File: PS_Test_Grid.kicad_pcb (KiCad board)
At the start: 2 copper layers, 51 parts, among them J1 CONN_01X03, J10 CONN_01X01, J2 CONN_01X01, J3 CONN_01X01, J4 CONN_01X01, J5 CONN_01X01, J6 CONN_01X03, J7 CONN_01X01, J8 CONN_01X01, J9 CONN_01X01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

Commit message: moved test points and cleaned schematic
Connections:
- C11 pad 2: Net-(C11-Pad2) -> /OUT_2-3
- C4 pad 2: Net-(C4-Pad2) -> /OUT_1-3
- J4 pad 1: /OUT_1-2 -> /OUT_1-3
- J9 pad 1: /OUT_2-2 -> /OUT_2-3
- R11 pad 1: Net-(C4-Pad2) -> /OUT_1-3
- R19 pad 1: Net-(C11-Pad2) -> /OUT_2-3
- U2 pad 1: Net-(C4-Pad2) -> /OUT_1-3
- U3 pad 1: Net-(C11-Pad2) -> /OUT_2-3

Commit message: upgraded to KiCad 5
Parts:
- R1, R2, R6, R7: footprint Capacitors_SMD:C_0603 -> Capacitors_SMD:C_0402
- R11: value R -> 330K
- R13, R14, R17: value R -> 100K
- R3, R4, R9: value R -> 220K
- moved U1 4.07 mm to (133.8, 88.5)

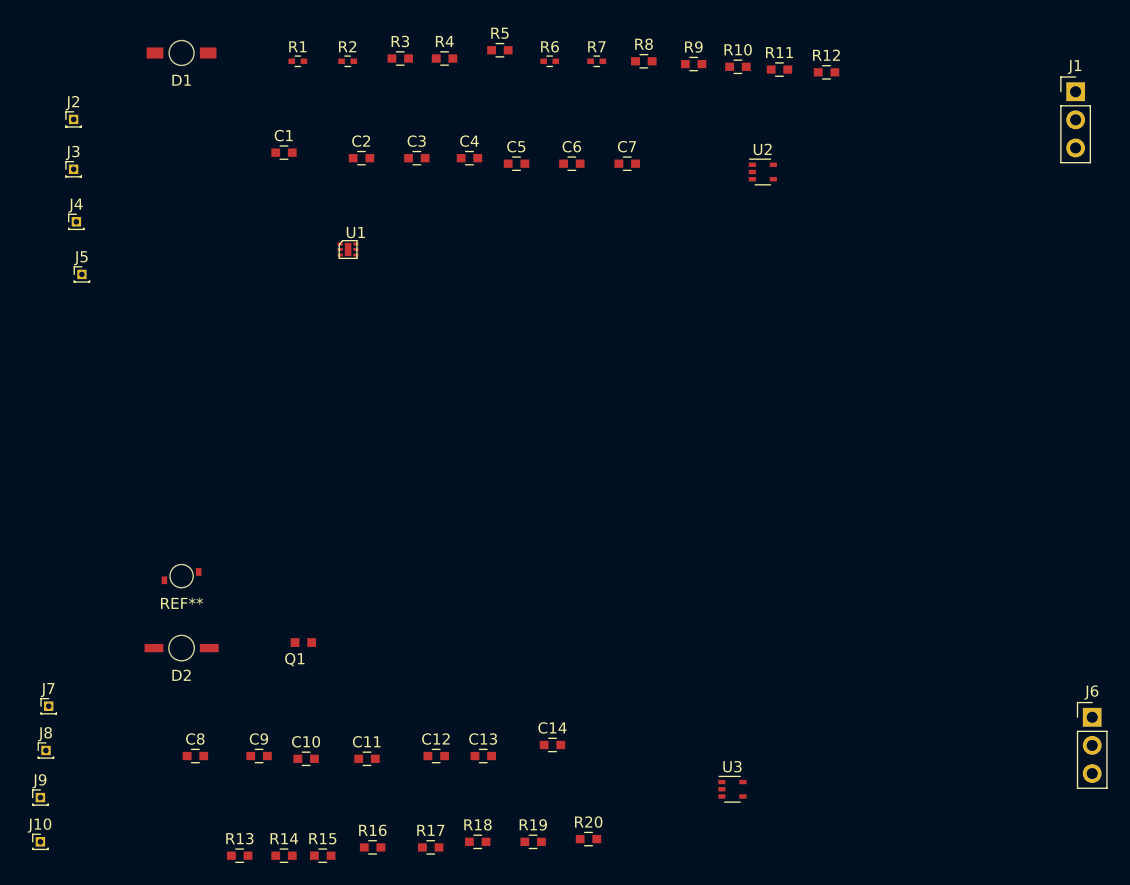
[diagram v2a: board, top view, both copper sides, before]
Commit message: Layout Circuit Add Protection Diode to Schem
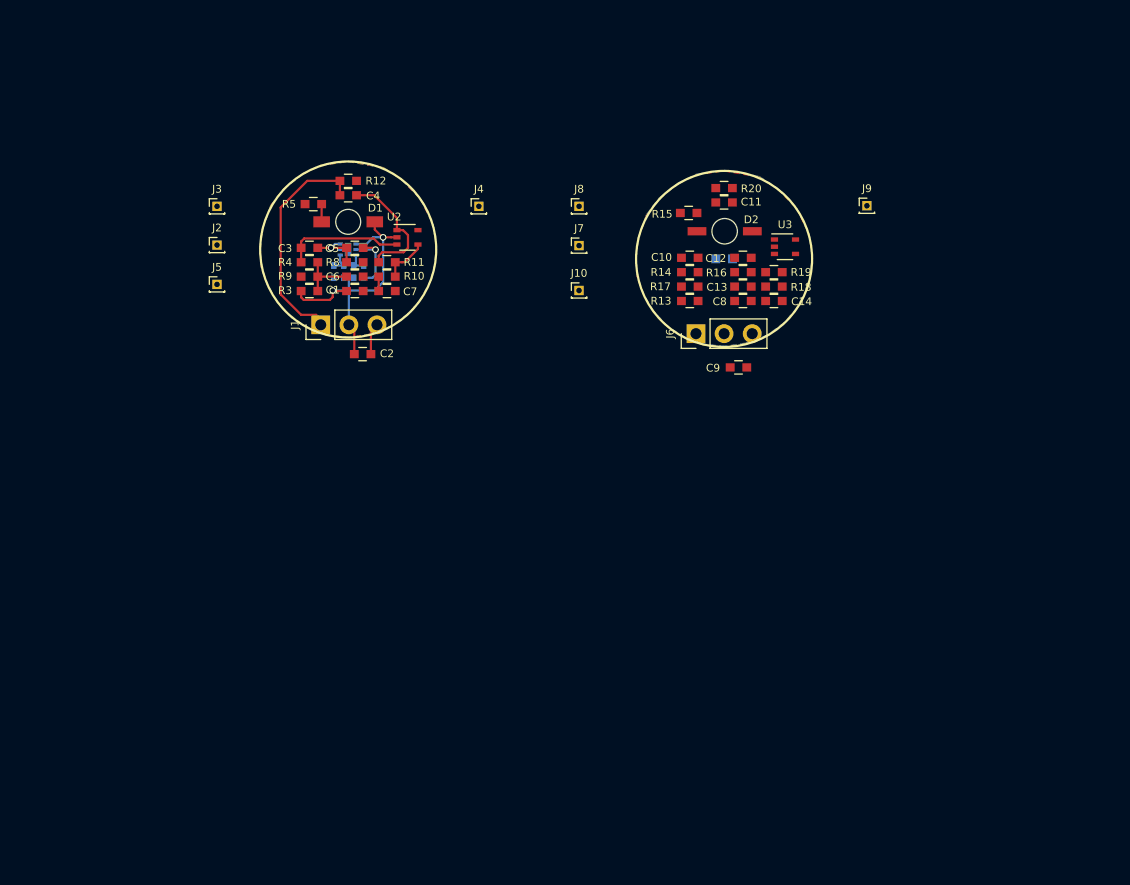
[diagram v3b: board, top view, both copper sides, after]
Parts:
- removed REF**: LSP47F LED, Solutions:LSP47F_LED
- Q1, R1, R2, R6, R7, U1: moved to B.Cu
- moved J9 91.8 mm to (180.7, 84.5)
- moved J1 71.4 mm to (131.3, 95.3), turned to 90 degrees
- moved J10 69.6 mm to (154.7, 92.2)
- moved J8 68.8 mm to (154.7, 84.6)
- moved R15 66.8 mm to (164.6, 85.2), turned to 180 degrees
- moved R13 64.5 mm to (164.7, 93.2)
- moved C8 64.3 mm to (169.4, 93.2)
- moved R14 64.2 mm to (164.7, 90.5)
- moved J7 63.4 mm to (154.7, 88.2)
- moved D2 61.8 mm to (167.8, 86.8)
- moved R16 61.8 mm to (169.4, 90.5)
- moved R20 60.1 mm to (167.8, 83.0)
- moved C11 59.7 mm to (167.8, 84.2)
- moved C10 57.0 mm to (164.7, 89.2)
- moved R18 56.8 mm to (172.2, 91.8), turned to 180 degrees
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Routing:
- net VDD: track 0.00 -> 28.5 mm, vias 0 -> 2
- net /S_1: track 0.00 -> 20.5 mm
- net /OUT_1-3: track 0.00 -> 11.5 mm
- net /OUT_1-2: track 0.00 -> 10.9 mm
- net GND: track 0.00 -> 9.28 mm, vias 0 -> 1
- net Net-(C6-Pad1): track 0.00 -> 5.20 mm
- net /OUT_1-1: track 0.00 -> 4.87 mm, vias 0 -> 1
- net Net-(R10-Pad1): track 0.00 -> 4.25 mm
- net Net-(R2-Pad2): track 0.00 -> 1.98 mm
- net Net-(R1-Pad2): track 0.00 -> 1.93 mm
- net Net-(D1-Pad1): track 0.00 -> 1.60 mm
- net Net-(C7-Pad1): track 0.00 -> 1.30 mm
- added copper zone on B.Cu, net GND
- added copper zone on F.Cu, net GND

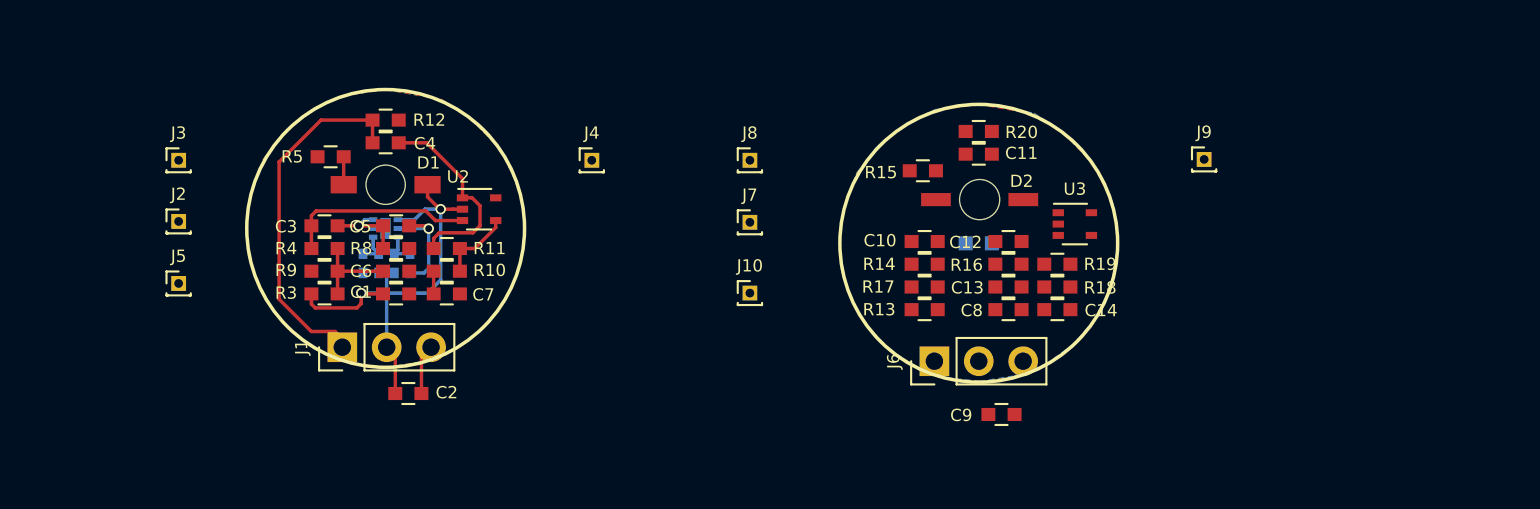
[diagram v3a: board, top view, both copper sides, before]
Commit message: laid out all drc pass
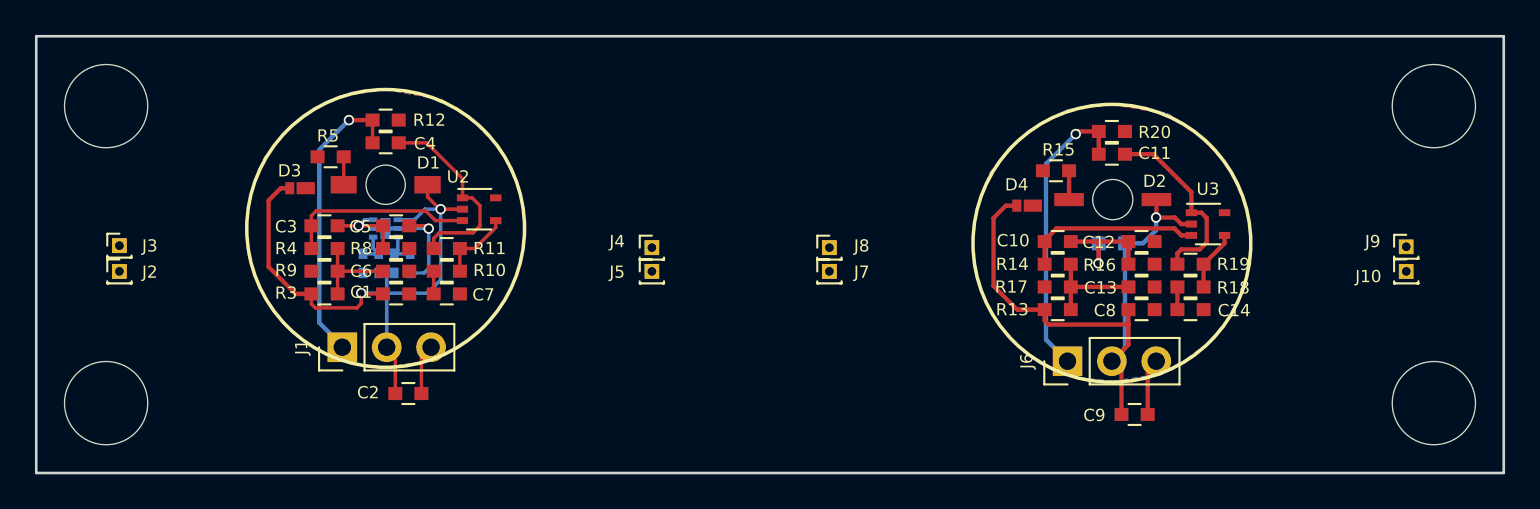
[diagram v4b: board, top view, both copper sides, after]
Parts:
- added D3: D_ALT, Solutions:NSR20F30NXT5G_DIODE, F.Cu at (128.9, 86.2)
- added D4: D_ALT, Solutions:NSR20F30NXT5G_DIODE, F.Cu at (170.5, 87.2)
- added REF**: NPTH_1.875MM, Solutions:NPTH_.1875_mil, F.Cu at (193.8, 98.5)
- added REF**: NPTH_1.875MM, Solutions:NPTH_.1875_mil, F.Cu at (193.8, 81.5)
- added REF**: NPTH_1.875MM, Solutions:NPTH_.1875_mil, F.Cu at (117.8, 81.5)
- added REF**: NPTH_1.875MM, Solutions:NPTH_.1875_mil, F.Cu at (117.8, 98.5)
- moved J10 37.6 mm to (192.2, 91.0)
- moved J5 27.1 mm to (149.0, 91.0)
- moved J9 12.6 mm to (192.2, 89.5)
- moved C10 7.62 mm to (172.3, 89.2)
- moved C11 7.62 mm to (175.4, 84.2)
- moved C12 7.62 mm to (177.1, 89.2)
- moved C13 7.62 mm to (177.1, 91.8)
- moved C14 7.62 mm to (179.9, 93.2)
- moved C8 7.62 mm to (177.1, 93.2)
- moved J6 7.62 mm to (172.8, 96.1)
- moved Q1 7.62 mm to (176.1, 89.3)
- moved R13 7.62 mm to (172.3, 93.2)
- moved R14 7.62 mm to (172.3, 90.5)
- moved R16 7.62 mm to (177.1, 90.5)
- moved R17 7.62 mm to (172.3, 91.8)
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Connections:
- U1 pad 7: (no net) -> GND
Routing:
- net VPP: track 0.00 -> 34.2 mm, vias 0 -> 1
- net /S_2: track 0.00 -> 16.9 mm, vias 0 -> 1
- net /OUT_2-3: track 0.00 -> 10.8 mm
- net /OUT_2-2: track 0.00 -> 10.2 mm
- net VDD: track 28.5 -> 36.9 mm
- net /OUT_2-1: track 0.00 -> 7.01 mm, vias 0 -> 1
- net Net-(C13-Pad1): track 0.00 -> 5.90 mm
- net /S_1: track 20.5 -> 16.9 mm, vias 0 -> 1
- net Net-(R18-Pad1): track 0.00 -> 3.45 mm
- net GNDD: track 0.00 -> 3.25 mm
- net Net-(D2-Pad1): track 0.00 -> 1.65 mm
- net Net-(C14-Pad1): track 0.00 -> 1.30 mm
- net GND: track 9.28 -> 9.99 mm
- added copper zone on B.Cu, net GNDD
- added copper zone on F.Cu, net GNDD
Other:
- board outline added: 84 x 25 mm
- board text added: "G V S"
- board text added: "GND"
- board text added: "OUT 1"
- board text added: "OUT 2"
- board text added: "OUT 3"

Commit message: adjusted protection diode. Reroute
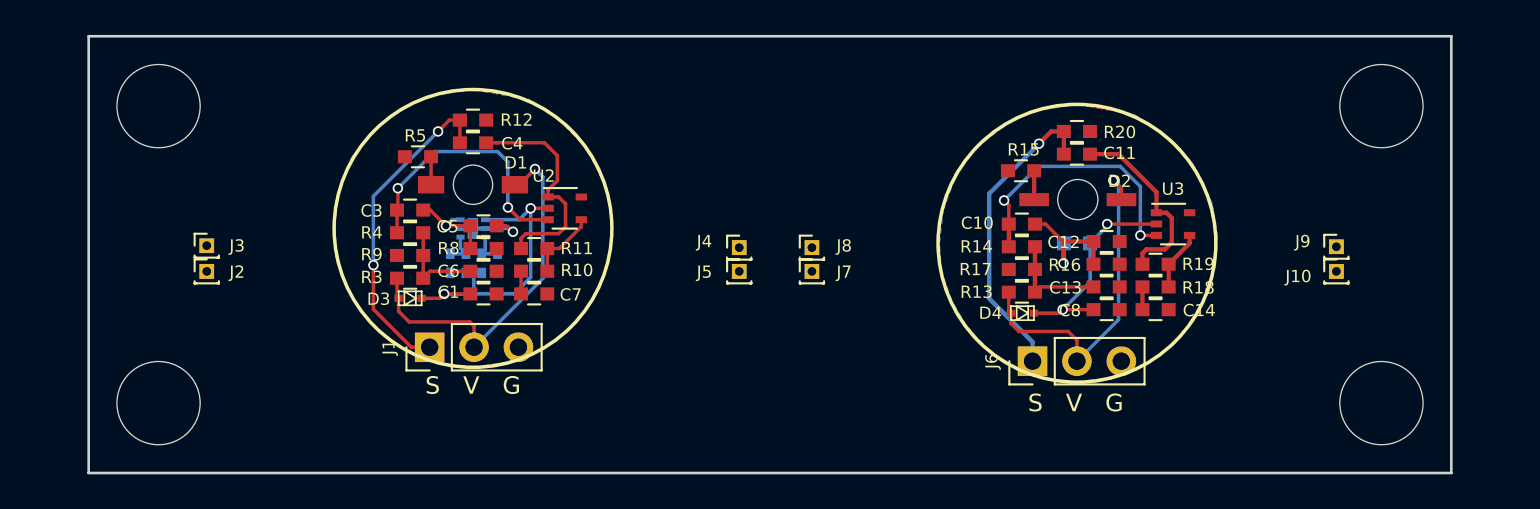
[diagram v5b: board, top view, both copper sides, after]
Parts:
- removed C2, C9: C, Capacitors_SMD:C_0603
- removed the REF** at (117.8, 81.5)
- removed the REF** at (117.8, 98.5)
- added REF**: NPTH_1.875MM, Solutions:NPTH_.1875_mil, F.Cu at (120.8, 81.5)
- added REF**: NPTH_1.875MM, Solutions:NPTH_.1875_mil, F.Cu at (120.8, 98.5)
- D3, D4: footprint Solutions:NSR20F30NXT5G_DIODE -> Solutions:RB751S40T5G_DIODE
- moved D3 8.91 mm to (135.2, 92.5), turned to 180 degrees
- moved D4 6.16 mm to (170.2, 93.3), turned to 180 degrees
- moved C1 5.00 mm to (139.4, 92.2)
- moved C4 5.00 mm to (138.8, 83.6)
- moved C5 5.00 mm to (139.4, 88.3)
- moved C6 5.00 mm to (139.4, 91.0)
- moved C7 5.00 mm to (142.3, 92.2)
- moved D1 5.00 mm to (138.8, 86.0)
- moved J1 5.00 mm to (136.3, 95.3)
- moved J2 5.00 mm to (123.6, 91.0)
- moved J3 5.00 mm to (123.6, 89.5)
- moved J4 5.00 mm to (154.0, 89.6)
- moved J5 5.00 mm to (154.0, 91.0)
- moved R1 5.00 mm to (139.3, 90.5)
- moved R10 5.00 mm to (142.3, 91.0)
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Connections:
- C1 pad 1: VDD -> /DVDD
- C8 pad 1: VPP -> /DVPP
- D3 pad 1: VDD -> /DVDD
- D3 pad 2: GND -> VDD
- D4 pad 1: VPP -> /DVPP
- D4 pad 2: GNDD -> VPP
- Q1 pad 1: VPP -> /DVPP
- R1 pad 1: VDD -> /DVDD
- R2 pad 1: VDD -> /DVDD
- U1 pad 1: VDD -> /DVDD
- U1 pad 7: GND -> (no net)
- U2 pad 2: VDD -> /DVDD
- U3 pad 2: VPP -> /DVPP
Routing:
- net /DVDD: track 0.00 -> 18.3 mm, vias 0 -> 2
- net VDD: track 36.9 -> 21.3 mm, vias 2 -> 1
- net VPP: track 34.2 -> 20.0 mm
- net /DVPP: track 0.00 -> 12.3 mm, vias 0 -> 2
- net GND: track 9.99 -> 4.26 mm
- net /OUT_2-2: track 10.2 -> 15.6 mm, vias 0 -> 2
- net /OUT_1-2: track 10.9 -> 15.2 mm, vias 0 -> 2
- net GNDD: track 3.25 -> 0.00 mm
- net /S_1: track 16.9 -> 19.0 mm, vias 1 -> 2
- net /OUT_1-3: track 11.5 -> 12.8 mm
- net /S_2: track 16.9 -> 17.7 mm
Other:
- board size 84 x 25 mm -> 78 x 25 mm
- board text added: "PULSE SENSOR V3 TEST GRID 12/18"
- board text added: "S V G"
- board text removed: "G V S"

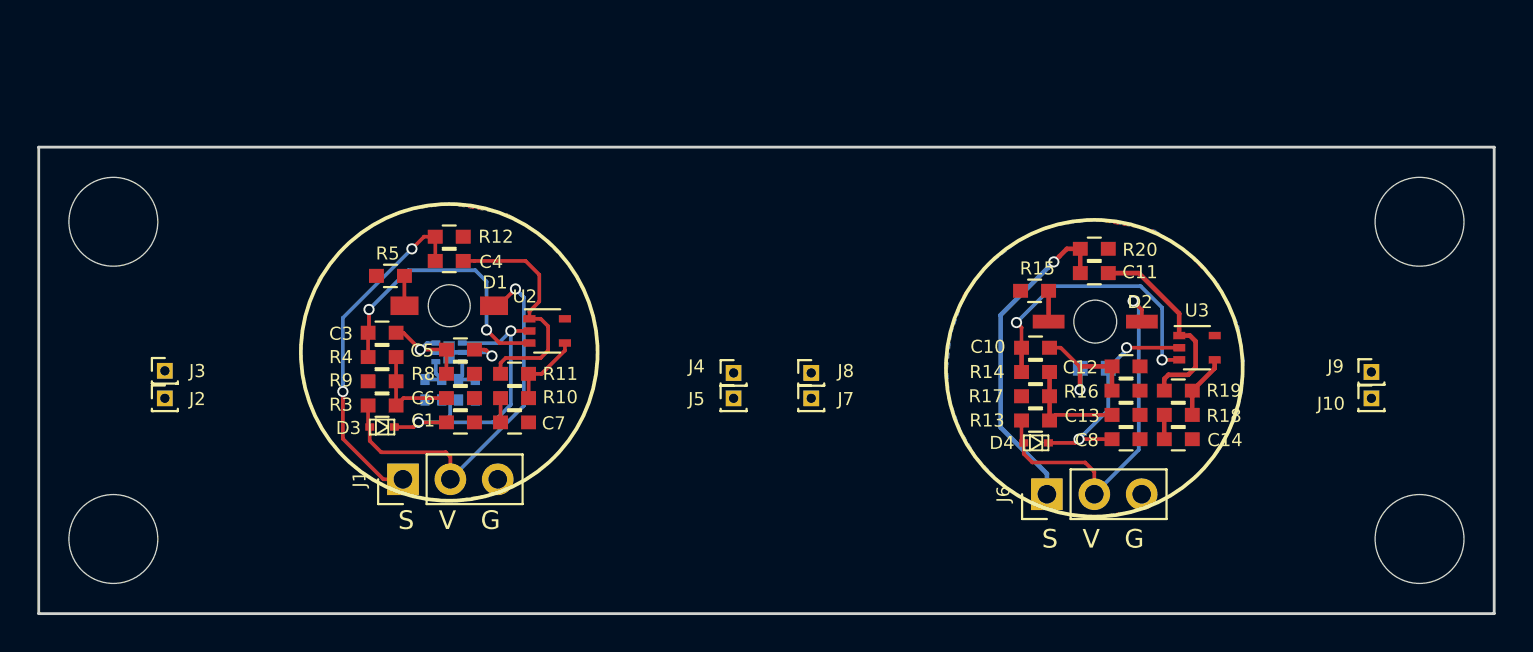
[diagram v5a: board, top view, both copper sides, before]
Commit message: added dual op amp circuit
ready to be laid out
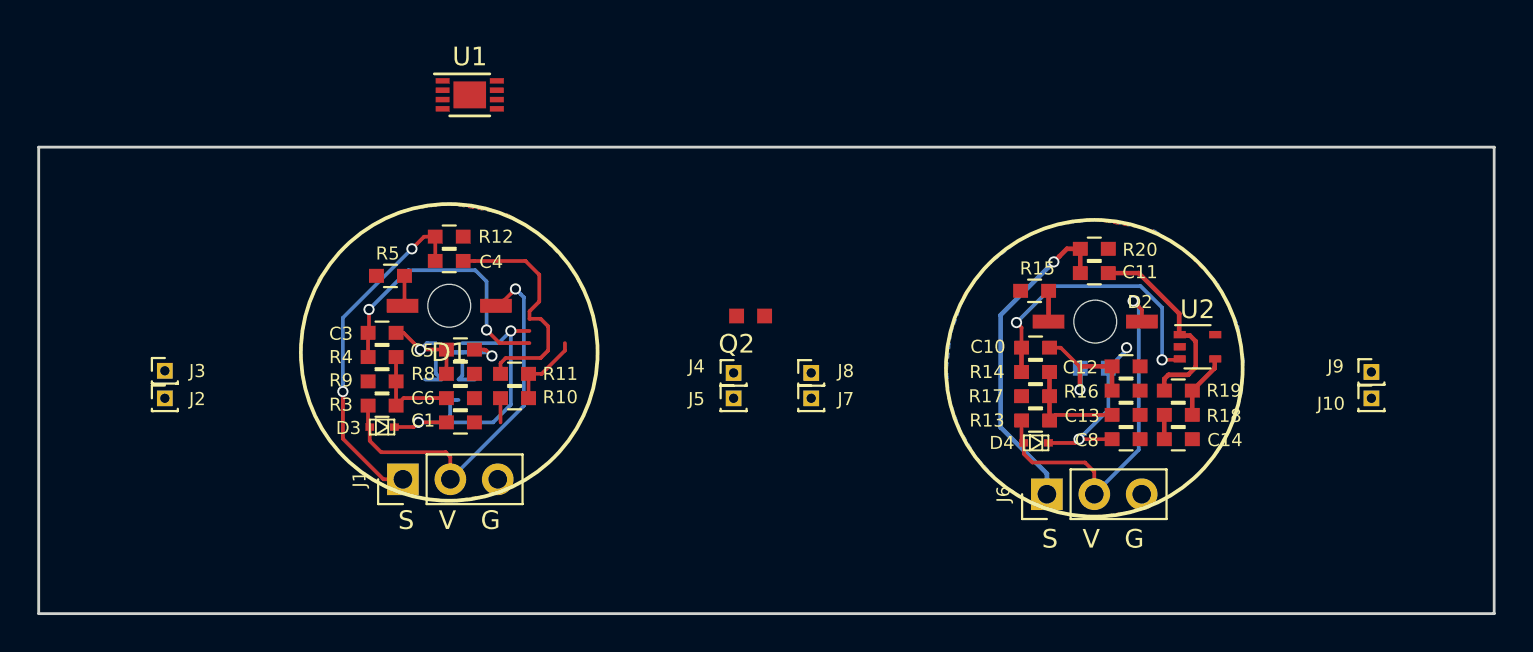
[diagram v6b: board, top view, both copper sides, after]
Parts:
- removed C7: C, Capacitors_SMD:C_0603
- removed R1, R2, R6, R7: R, Capacitors_SMD:C_0402
- removed REF** (x4): NPTH_1.875MM, Solutions:NPTH_.1875_mil
- removed U3: MCP6001R, TO_SOT_Packages_SMD:SOT-353_SC-70-5
- added Q2: PhotoTransistor, Solutions:EAALSTIC1708A0, F.Cu at (154.2, 86.5)
- D1: footprint Solutions:AM2520ZGC09_LED -> Solutions:VLD1235R_LED
- U1: value NOA1212 -> MCP6002-xMC; footprint Solutions:NOA1212CUTAG -> Package_DFN_QFN:DFN-8-1EP_3x2mm_P0.5mm_EP1.75x1.45mm; moved to F.Cu
- U2: value MCP6001R -> MCP6001x-LT; footprint TO_SOT_Packages_SMD:SOT-353_SC-70-5 -> Package_TO_SOT_SMD:SOT-353_SC-70-5
- moved U2 34.9 mm to (178.9, 88.2)
- moved U1 13.8 mm to (139.9, 74.7), turned to 0 degrees
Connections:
- R10 pad 2: Net-(C7-Pad1) -> GNDREF
- R3 pad 1: VDD -> /DVDD
- R4 pad 1: /OUT_1-2 -> GNDREF
- R4 pad 2: Net-(C6-Pad1) -> /OUT_1-2
- U1 pad 1: /DVDD -> GNDREF
- U1 pad 2: GND -> GNDREF
- U1 pad 3: Net-(R1-Pad2) -> Net-(C6-Pad1)
- U1 pad 4: Net-(R2-Pad2) -> GND
- U1 pad 5: Net-(U1-Pad5) -> /OUT_1-2
- U1 pad 6: /OUT_1-1 -> Net-(R10-Pad1)
- U1 pad 7: (no net) -> /OUT_1-3
- U2 pad 1: /OUT_1-3 -> /OUT_2-3
- U2 pad 2: /DVDD -> GNDD
- U2 pad 3: /OUT_1-2 -> /OUT_2-2
- U2 pad 4: Net-(R10-Pad1) -> Net-(R18-Pad1)
- U2 pad 5: GND -> /DVPP
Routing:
- net /DVPP: track 12.3 -> 9.45 mm
- net Net-(C7-Pad1): track 1.30 -> 0.00 mm
- net GNDREF: track 0.00 -> 1.30 mm
